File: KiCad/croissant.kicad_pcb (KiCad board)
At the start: 2 copper layers, 149.8 x 90.3 mm, 53 parts, among them J1 USB_C_Receptacle_PowerOnly_6P, Q1 NMOS, SW1 SW_SPDT, U1 NE556, U2 TL064

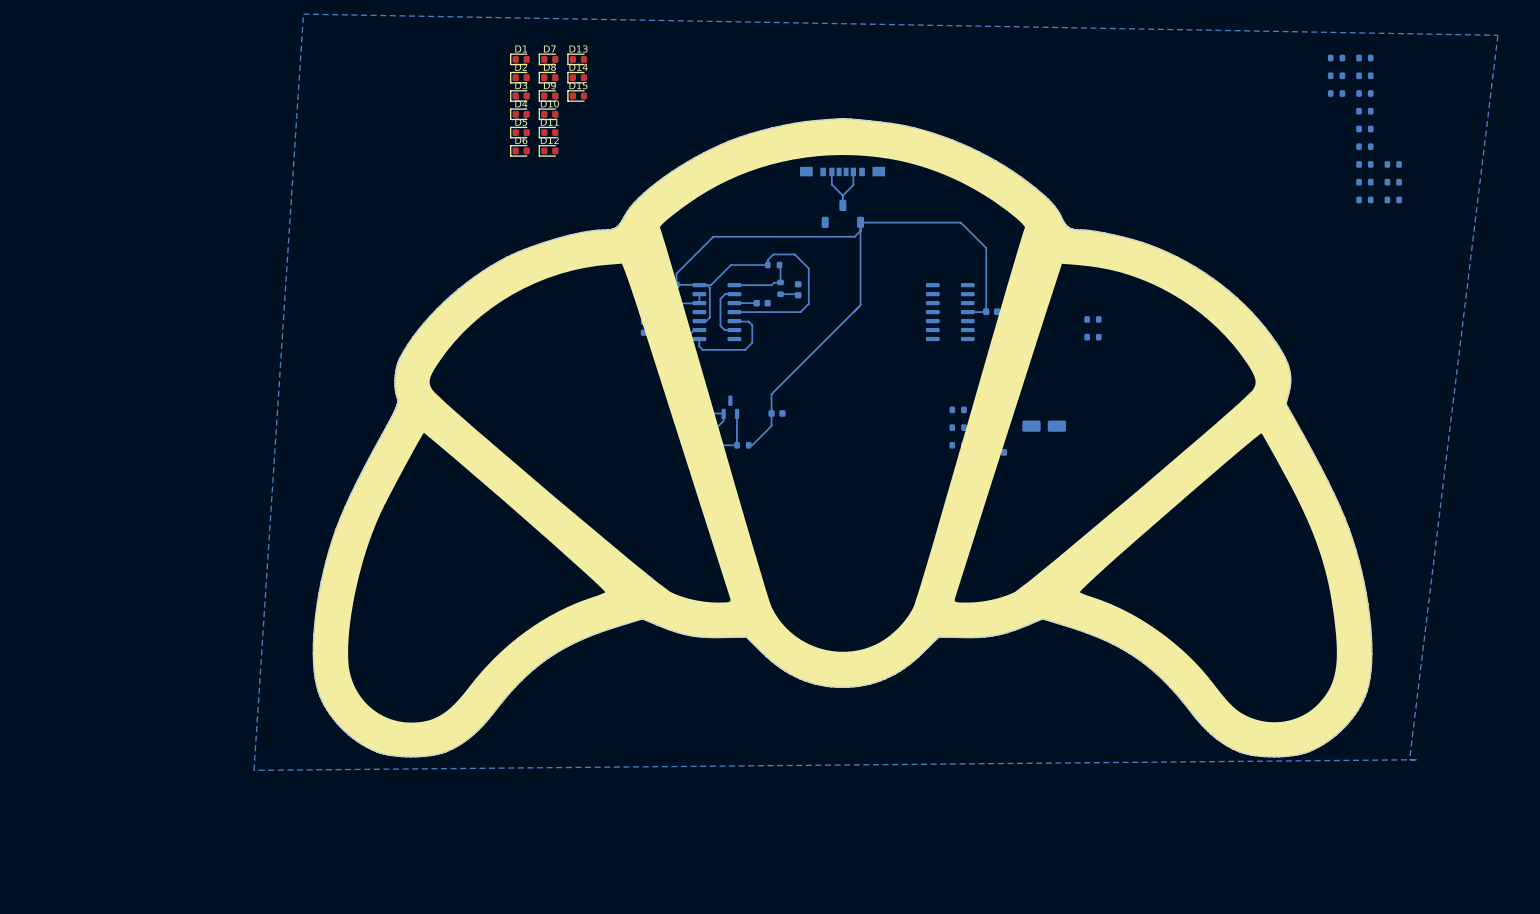
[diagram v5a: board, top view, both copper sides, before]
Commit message: Placed LEDs
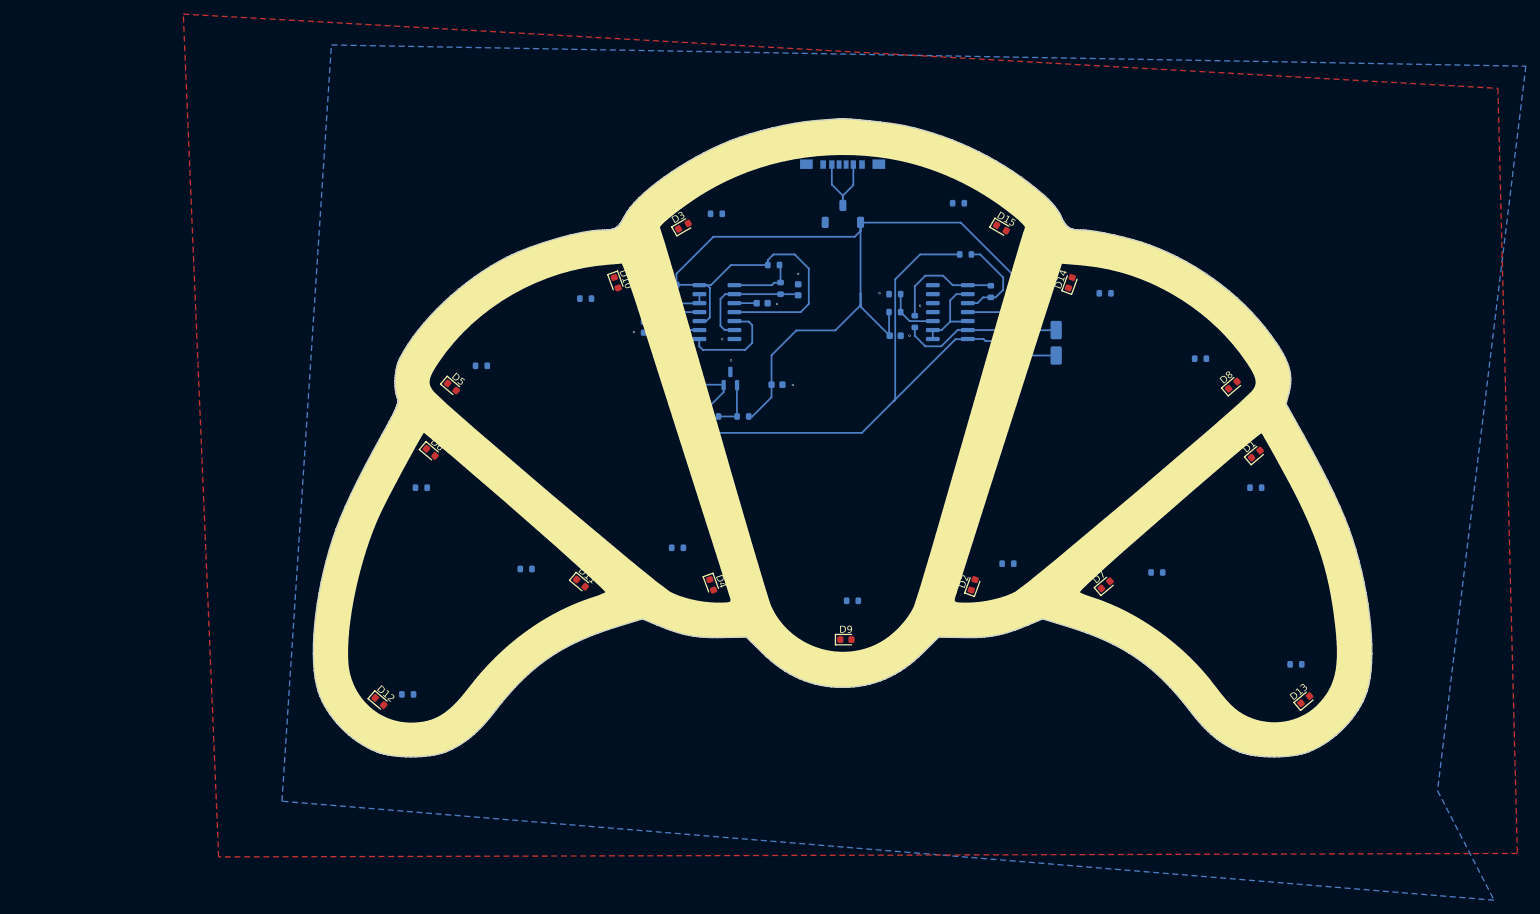
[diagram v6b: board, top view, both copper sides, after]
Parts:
- added C9: 0.1u, Capacitor_SMD:C_0603_1608Metric, B.Cu at (152.2, 77.0)
- moved R20 152.4 mm to (83.2, 127.8)
- moved R14 144.7 mm to (85.2, 98.5)
- moved D13 137.1 mm to (210.2, 128.5), turned to 40 degrees
- moved R13 131.6 mm to (93.7, 81.2)
- moved R19 130.7 mm to (100.0, 110.0)
- moved R12 119.4 mm to (121.4, 107.0)
- moved D1 118.0 mm to (203.2, 93.8), turned to 40 degrees
- moved R18 111.9 mm to (108.4, 71.8)
- moved D7 108.2 mm to (182.0, 112.2), turned to 40 degrees
- moved D8 106.0 mm to (200.0, 84.0), turned to 40 degrees
- moved R17 96.9 mm to (146.2, 114.5)
- moved D2 96.1 mm to (163.2, 112.2), turned to 70 degrees
- moved R11 95.8 mm to (126.9, 59.8)
- moved D9 87.6 mm to (145.2, 120.0)
- moved R21 86.0 mm to (208.9, 123.5)
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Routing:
- net /TriangleOut: track 0.00 -> 107.1 mm
- net Net-(U2B--): track 0.00 -> 22.8 mm
- net Net-(R6-Pad1): track 0.00 -> 16.1 mm
- net +5V: track 152.0 -> 167.6 mm
- net Net-(U2A-+): track 0.00 -> 13.4 mm
- net /VGND: track 0.00 -> 12.6 mm
- net Net-(U2C-+): track 0.00 -> 7.61 mm
- net Net-(U1A-THR): track 10.8 -> 17.4 mm
- net Net-(Q1-G): track 21.9 -> 18.7 mm
- net Net-(SW1-B): track 9.33 -> 11.4 mm
- net GND: vias 0 -> 12
- added copper zone on F.Cu, net GND

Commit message: Fix via sizes
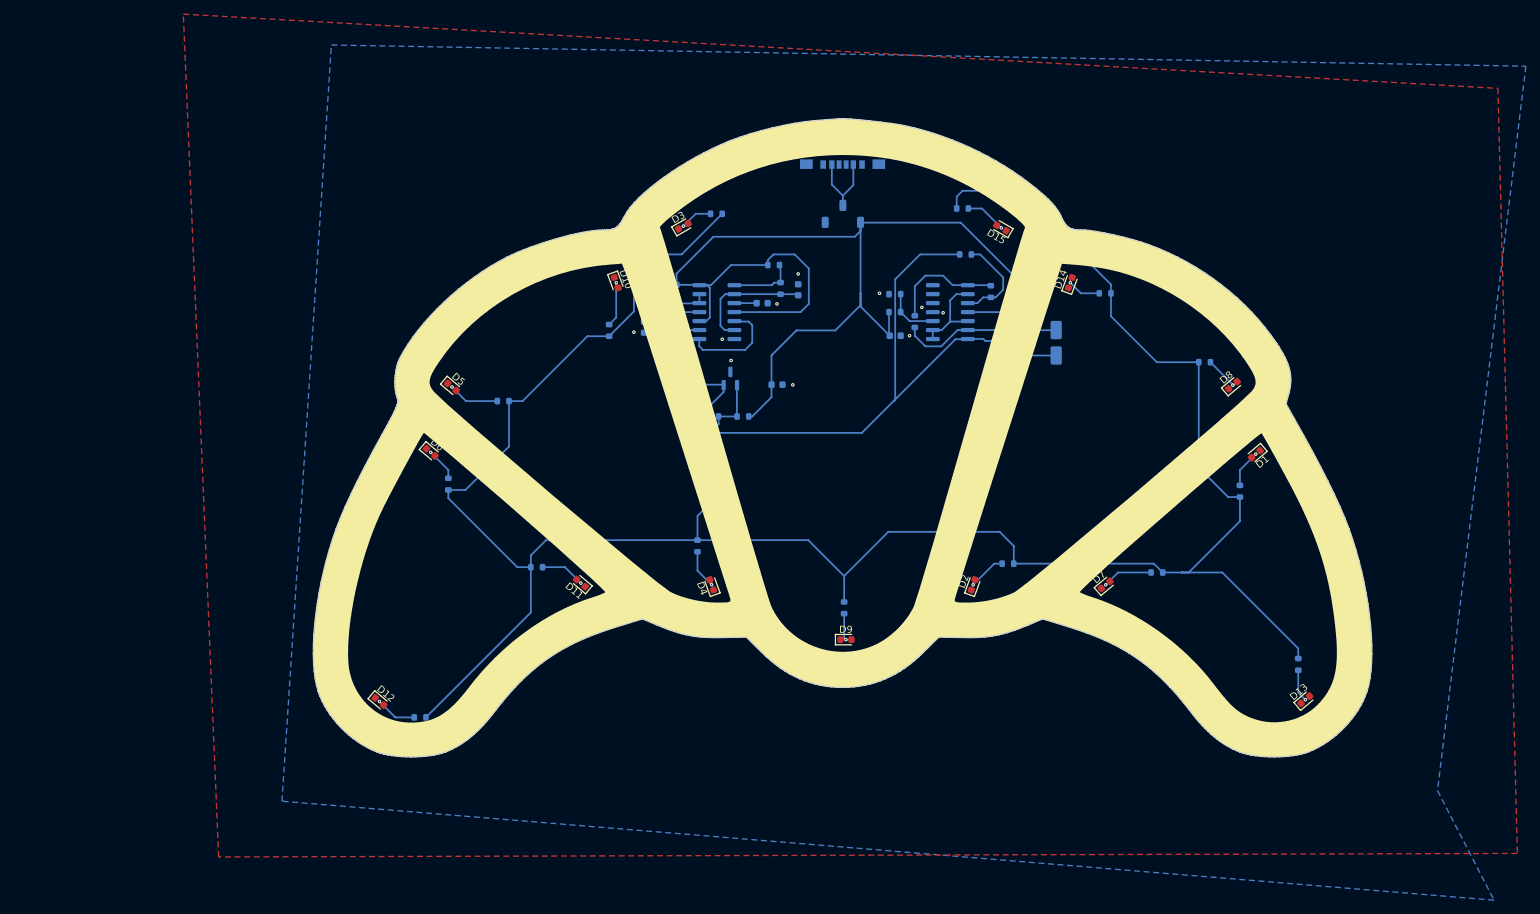
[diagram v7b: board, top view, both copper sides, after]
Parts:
- moved R13 5.87 mm to (96.8, 86.2)
- moved R18 5.60 mm to (111.8, 76.2), turned to 90 degrees
- moved R14 3.86 mm to (89.0, 98.0), turned to 90 degrees
- moved R20 3.69 mm to (85.0, 131.0)
- moved R12 2.84 mm to (124.2, 106.8), turned to -90 degrees
- moved R9 2.30 mm to (201.0, 99.0), turned to 90 degrees
- moved R17 1.54 mm to (145.0, 115.5), turned to -90 degrees
- moved R19 1.52 mm to (101.5, 109.8), turned to 0 degrees
- moved R23 0.95 mm to (161.8, 59.0), turned to 0 degrees
- moved R16 0.76 mm to (196.0, 80.8), turned to 0 degrees
- moved R21 0.32 mm to (209.2, 123.5), turned to -90 degrees
- turned D1 to -140 degrees
- turned D11 to 140 degrees
- turned D15 to 150 degrees
- turned D4 to 110 degrees
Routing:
- net /PWMOut: track 7.02 -> 346.8 mm, vias 0 -> 2
- net Net-(D5-A): track 0.00 -> 8.07 mm, vias 0 -> 1
- net Net-(D7-A): track 0.00 -> 7.96 mm, vias 0 -> 1
- net Net-(D10-A): track 0.00 -> 7.19 mm, vias 0 -> 1
- net Net-(D11-A): track 0.00 -> 7.17 mm, vias 0 -> 1
- net Net-(D15-A): track 0.00 -> 6.66 mm, vias 0 -> 1
- net Net-(D4-A): track 0.00 -> 6.35 mm, vias 0 -> 1
- net Net-(D12-A): track 0.00 -> 6.21 mm, vias 0 -> 1
- net Net-(D2-A): track 0.00 -> 6.19 mm, vias 0 -> 1
- net Net-(D1-A): track 0.00 -> 6.17 mm, vias 0 -> 1
- net Net-(D14-A): track 0.00 -> 5.57 mm, vias 0 -> 1
- net Net-(D6-A): track 0.00 -> 5.52 mm, vias 0 -> 1
- net Net-(D3-A): track 0.00 -> 5.42 mm, vias 0 -> 1
- net Net-(D13-A): track 0.00 -> 5.40 mm, vias 0 -> 1
- net Net-(D8-A): track 0.00 -> 5.38 mm, vias 0 -> 1
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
